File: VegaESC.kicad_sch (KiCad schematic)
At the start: 110 parts, among them J1 A, J2 BATT, J3 Conn_01x05, J4 B, J5 GND, J6 C, P1 SM08B-SRSS-TB, Q1 Q_NMOS_GDS, Q2 Q_NMOS_GDS, Q3 Q_NMOS_GDS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

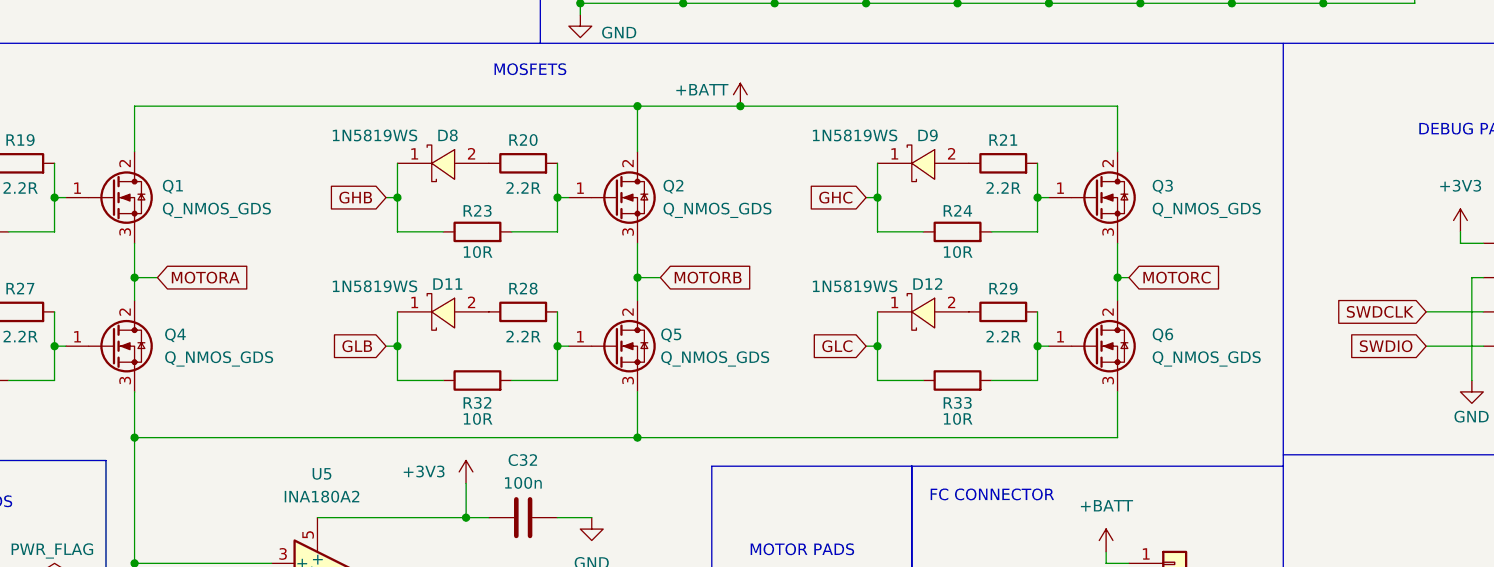
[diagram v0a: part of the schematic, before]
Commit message: Switch MOSFETs (Q1-Q6) to NTMFS5C430NLT1G in schematic and BOM files
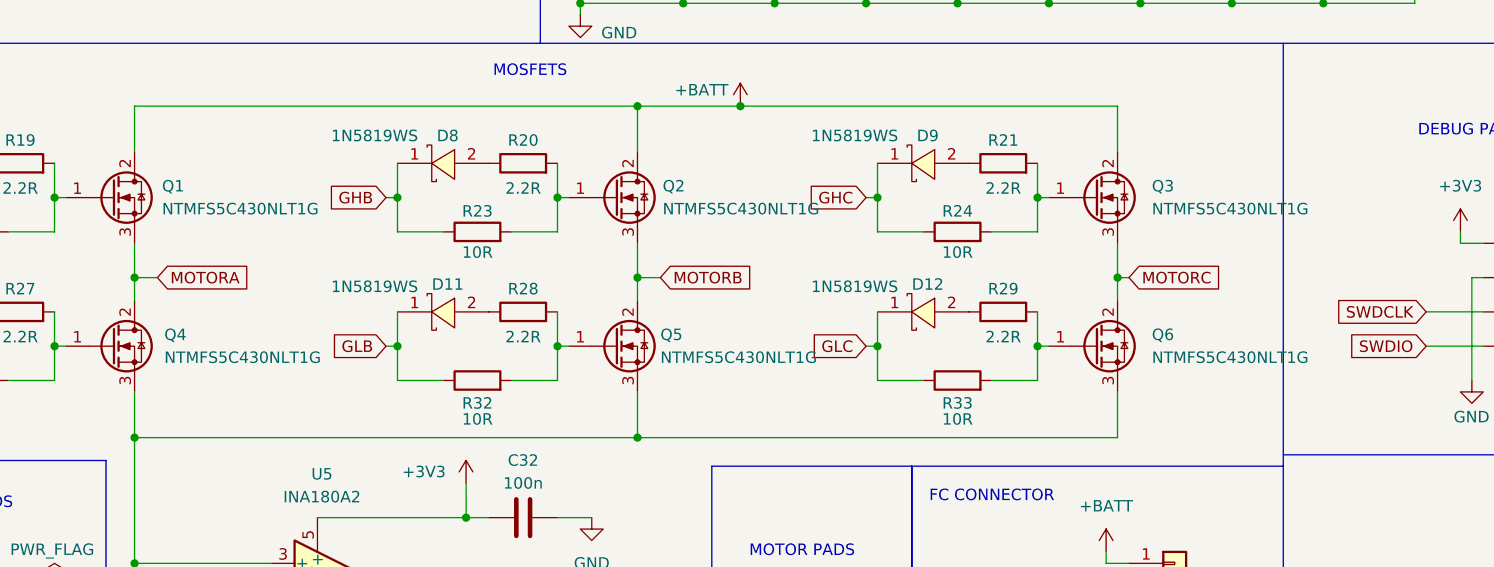
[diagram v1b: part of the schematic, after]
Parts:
- Q1, Q2, Q3, Q4, Q5, Q6: value Q_NMOS_GDS -> NTMFS5C430NLT1G; footprint easyeda2kicad:POWERVDFN-8_L6.2-W5.2-P1.27-LS6.0-BL -> easyeda2kicad:DFN-5_L4.9-W5.9-P1.27-LS6.2-BL; MPN JMSH0401AGQ -> NTMFS5C430NLT1G; Manufacturer Jiangsu JieJie Microelectronics -> onsemi; lcsc C7527437 -> C194661
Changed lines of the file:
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@@
 			)
 		)
-		(property "Value" "Q_NMOS_GDS"
+		(property "Value" "NTMFS5C430NLT1G"
 			(at 107.95 154.94 0)
 			(show_name no)
@@
 			)
 		)
-		(property "Footprint" "easyeda2kicad:POWERVDFN-8_L6.2-W5.2-P1.27-LS6.0-BL"
+		(property "Footprint" "easyeda2kicad:DFN-5_L4.9-W5.9-P1.27-LS6.2-BL"
 			(at 107.95 151.13 0)
 			(hide yes)
@@
 			)
 		)
-		(property "Datasheet" "https://datasheet.lcsc.com/datasheet/pdf/279cd1f797cb03731ab717b6e54fa0a8.pdf?productCode=C7527437"
+		(property "Datasheet" "https://www.onsemi.com/products/discrete-power-modules/mosfets/ntmfs5c430nl"
 			(at 102.87 153.67 0)
 			(hide yes)
@@
 			)
 		)
-		(property "Description" "N-MOSFET transistor, gate/drain/source"
+		(property "Description" "N-channel 40V 200A 1.4mΩ@10V DFN5(5x6) MOSFET"
 			(at 102.87 153.67 0)
 			(hide yes)
@@
 			)
 		)
-		(property "Manufacturer" "Jiangsu JieJie Microelectronics"
+		(property "Manufacturer" "onsemi"
 			(at 0 0 0)
 			(hide yes)
@@
 			)
 		)
-		(property "MPN" "JMSH0401AGQ"
+		(property "MPN" "NTMFS5C430NLT1G"
 			(at 0 0 0)
 			(hide yes)
@@
 			)
 		)
-		(property "lcsc" "C7527437"
+		(property "lcsc" "C194661"
 			(at 0 0 0)
 			(hide yes)
@@
 			)
 		)
-		(property "Value" "Q_NMOS_GDS"
+		(property "Value" "NTMFS5C430NLT1G"
 			(at 52.578 138.43 0)
 			(show_name no)
@@
 			)
 		)
-		(property "Footprint" "easyeda2kicad:POWERVDFN-8_L6.2-W5.2-P1.27-LS6.0-BL"
+		(property "Footprint" "easyeda2kicad:DFN-5_L4.9-W5.9-P1.27-LS6.2-BL"
 			(at 52.07 134.62 0)
 			(hide yes)
@@
 			)
 		)
-		(property "Datasheet" "https://datasheet.lcsc.com/datasheet/pdf/279cd1f797cb03731ab717b6e54fa0a8.pdf?productCode=C7527437"
+		(property "Datasheet" "https://www.onsemi.com/products/discrete-power-modules/mosfets/ntmfs5c430nl"
 			(at 46.99 137.16 0)
 			(hide yes)
@@
 			)
 		)
-		(property "Description" "N-MOSFET transistor, gate/drain/source"
+		(property "Description" "N-channel 40V 200A 1.4mΩ@10V DFN5(5x6) MOSFET"
 			(at 46.99 137.16 0)
 			(hide yes)
@@
 			)
 		)
-		(property "Manufacturer" "Jiangsu JieJie Microelectronics"
+		(property "Manufacturer" "onsemi"
 			(at 0 0 0)
 			(hide yes)
@@
 			)
 		)
-		(property "MPN" "JMSH0401AGQ"
+		(property "MPN" "NTMFS5C430NLT1G"
 			(at 0 0 0)
 			(hide yes)
@@
 			)
 		)
-		(property "lcsc" "C7527437"
+		(property "lcsc" "C194661"
 			(at 0 0 0)
 			(hide yes)
@@
 			)
 		)
-		(property "Value" "Q_NMOS_GDS"
+		(property "Value" "NTMFS5C430NLT1G"
 			(at 52.832 154.94 0)
 			(show_name no)
@@
 			)
 		)
-		(property "Footprint" "easyeda2kicad:POWERVDFN-8_L6.2-W5.2-P1.27-LS6.0-BL"
+		(property "Footprint" "easyeda2kicad:DFN-5_L4.9-W5.9-P1.27-LS6.2-BL"
 			(at 52.07 151.13 0)
 			(hide yes)
@@
 			)
 		)
-		(property "Datasheet" "https://datasheet.lcsc.com/datasheet/pdf/279cd1f797cb03731ab717b6e54fa0a8.pdf?productCode=C7527437"
+		(property "Datasheet" "https://www.onsemi.com/products/discrete-power-modules/mosfets/ntmfs5c430nl"
 			(at 46.99 153.67 0)
 			(hide yes)
@@
 			)
 		)
-		(property "Description" "N-MOSFET transistor, gate/drain/source"
+		(property "Description" "N-channel 40V 200A 1.4mΩ@10V DFN5(5x6) MOSFET"
 			(at 46.99 153.67 0)
 			(hide yes)
@@
 			)
 		)
-		(property "Manufacturer" "Jiangsu JieJie Microelectronics"
+		(property "Manufacturer" "onsemi"
 			(at 0 0 0)
 			(hide yes)
@@
 			)
 		)
-		(property "MPN" "JMSH0401AGQ"
+		(property "MPN" "NTMFS5C430NLT1G"
 			(at 0 0 0)
 			(hide yes)
@@
 			)
 		)
-		(property "lcsc" "C7527437"
+		(property "lcsc" "C194661"
 			(at 0 0 0)
 			(hide yes)
@@
 			)
 		)
-		(property "Value" "Q_NMOS_GDS"
+		(property "Value" "NTMFS5C430NLT1G"
 			(at 162.56 138.4299 0)
 			(show_name no)
@@
 			)
 		)
-		(property "Footprint" "easyeda2kicad:POWERVDFN-8_L6.2-W5.2-P1.27-LS6.0-BL"
+		(property "Footprint" "easyeda2kicad:DFN-5_L4.9-W5.9-P1.27-LS6.2-BL"
 			(at 161.29 134.62 0)
 			(hide yes)
@@
 			)
 		)
-		(property "Datasheet" "https://datasheet.lcsc.com/datasheet/pdf/279cd1f797cb03731ab717b6e54fa0a8.pdf?productCode=C7527437"
+		(property "Datasheet" "https://www.onsemi.com/products/discrete-power-modules/mosfets/ntmfs5c430nl"
 			(at 156.21 137.16 0)
 			(hide yes)
@@
 			)
 		)
-		(property "Description" "N-MOSFET transistor, gate/drain/source"
+		(property "Description" "N-channel 40V 200A 1.4mΩ@10V DFN5(5x6) MOSFET"
 			(at 156.21 137.16 0)
 			(hide yes)
@@
 			)
 		)
-		(property "Manufacturer" "Jiangsu JieJie Microelectronics"
+		(property "Manufacturer" "onsemi"
 			(at 0 0 0)
 			(hide yes)
@@
 			)
 		)
-		(property "MPN" "JMSH0401AGQ"
+		(property "MPN" "NTMFS5C430NLT1G"
 			(at 0 0 0)
 			(hide yes)
@@
 			)
 		)
-		(property "lcsc" "C7527437"
+		(property "lcsc" "C194661"
 			(at 0 0 0)
 			(hide yes)
@@
 			)
 		)
-		(property "Value" "Q_NMOS_GDS"
+		(property "Value" "NTMFS5C430NLT1G"
 			(at 162.56 154.9399 0)
 			(show_name no)
@@
 			)
 		)
-		(property "Footprint" "easyeda2kicad:POWERVDFN-8_L6.2-W5.2-P1.27-LS6.0-BL"
+		(property "Footprint" "easyeda2kicad:DFN-5_L4.9-W5.9-P1.27-LS6.2-BL"
 			(at 161.29 151.13 0)
 			(hide yes)
@@
 			)
 		)
-		(property "Datasheet" "https://datasheet.lcsc.com/datasheet/pdf/279cd1f797cb03731ab717b6e54fa0a8.pdf?productCode=C7527437"
+		(property "Datasheet" "https://www.onsemi.com/products/discrete-power-modules/mosfets/ntmfs5c430nl"
 			(at 156.21 153.67 0)
 			(hide yes)
@@
 			)
 		)
-		(property "Description" "N-MOSFET transistor, gate/drain/source"
+		(property "Description" "N-channel 40V 200A 1.4mΩ@10V DFN5(5x6) MOSFET"
 			(at 156.21 153.67 0)
 			(hide yes)
@@
 			)
 		)
-		(property "Manufacturer" "Jiangsu JieJie Microelectronics"
+		(property "Manufacturer" "onsemi"
 			(at 0 0 0)
 			(hide yes)
@@
 			)
 		)
-		(property "MPN" "JMSH0401AGQ"
+		(property "MPN" "NTMFS5C430NLT1G"
 			(at 0 0 0)
 			(hide yes)
@@
 			)
 		)
-		(property "lcsc" "C7527437"
+		(property "lcsc" "C194661"
 			(at 0 0 0)
 			(hide yes)
@@
 			)
 		)
-		(property "Value" "Q_NMOS_GDS"
+		(property "Value" "NTMFS5C430NLT1G"
 			(at 108.204 138.43 0)
 			(show_name no)
@@
 			)
 		)
-		(property "Footprint" "easyeda2kicad:POWERVDFN-8_L6.2-W5.2-P1.27-LS6.0-BL"
+		(property "Footprint" "easyeda2kicad:DFN-5_L4.9-W5.9-P1.27-LS6.2-BL"
 			(at 107.95 134.62 0)
 			(hide yes)
@@
 			)
 		)
-		(property "Datasheet" "https://datasheet.lcsc.com/datasheet/pdf/279cd1f797cb03731ab717b6e54fa0a8.pdf?productCode=C7527437"
+		(property "Datasheet" "https://www.onsemi.com/products/discrete-power-modules/mosfets/ntmfs5c430nl"
 			(at 102.87 137.16 0)
 			(hide yes)
@@
 			)
 		)
-		(property "Description" "N-MOSFET transistor, gate/drain/source"
+		(property "Description" "N-channel 40V 200A 1.4mΩ@10V DFN5(5x6) MOSFET"
 			(at 102.87 137.16 0)
 			(hide yes)
@@
 			)
 		)
-		(property "Manufacturer" "Jiangsu JieJie Microelectronics"
+		(property "Manufacturer" "onsemi"
 			(at 0 0 0)
 			(hide yes)
@@
 			)
 		)
-		(property "MPN" "JMSH0401AGQ"
+		(property "MPN" "NTMFS5C430NLT1G"
 			(at 0 0 0)
 			(hide yes)
@@
 			)
 		)
-		(property "lcsc" "C7527437"
+		(property "lcsc" "C194661"
 			(at 0 0 0)
 			(hide yes)
